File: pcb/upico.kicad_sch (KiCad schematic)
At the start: 71 parts, among them J1 uConsoleEXT, J2 uPico Connect, J3 USB_C_Receptacle_USB2.0, J4 Camera, J5 uConsoleSpeaker, J6 uConsoleSpeaker, U1 W25Q32JVUX, U2 RP2040, U3 USBLC6-2P6, U4 USBLC6-2P6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

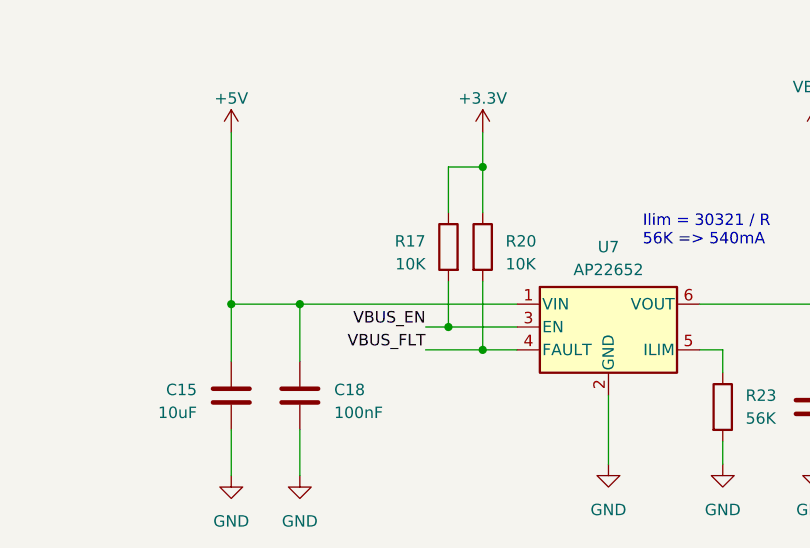
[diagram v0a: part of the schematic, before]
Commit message: invert power control signals
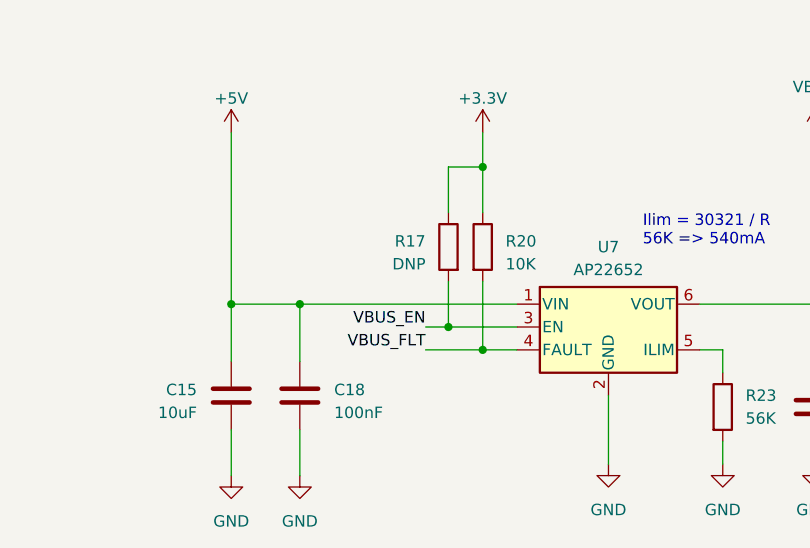
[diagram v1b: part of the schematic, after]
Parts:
- R17: value 10K -> DNP; PN C25744 -> (none)
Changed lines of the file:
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@@
       (effects (font (size 1.27 1.27)) (justify left))
     )
-    (property "Value" "10K" (at 340.36 55.245 0)
+    (property "Value" "DNP" (at 340.36 55.245 0)
       (effects (font (size 1.27 1.27)) (justify left))
     )
@@
       (effects (font (size 1.27 1.27)) hide)
     )
-    (property "PN" "C25744" (at 342.9 53.34 0)
+    (property "PN" "" (at 342.9 53.34 0)
       (effects (font (size 1.27 1.27)) hide)
     )

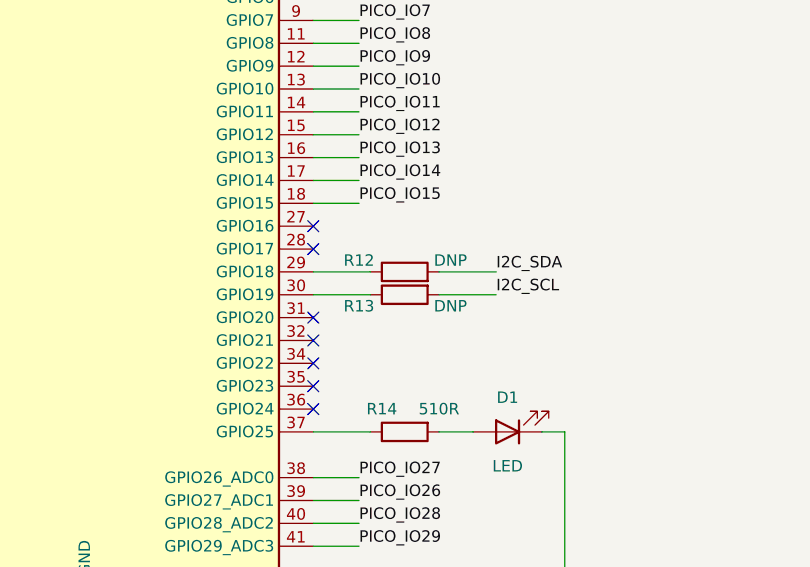
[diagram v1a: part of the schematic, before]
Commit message: pico auto mount
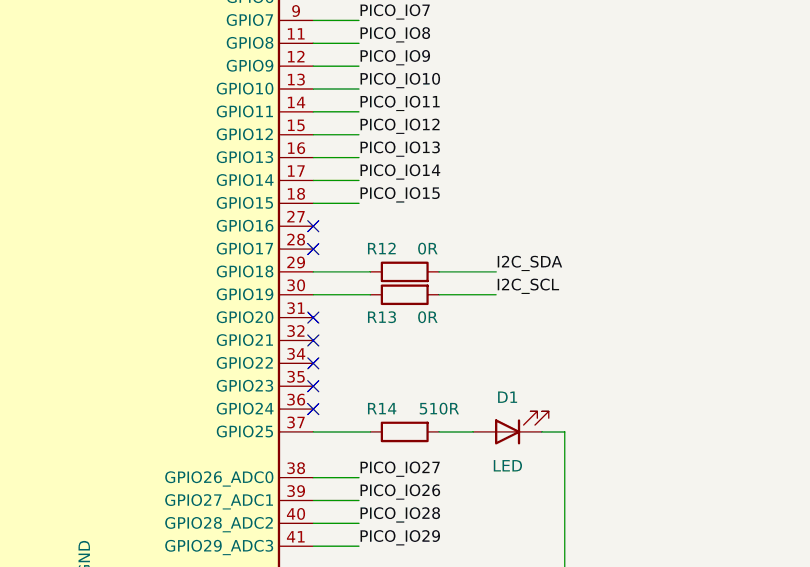
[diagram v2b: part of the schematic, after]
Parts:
- R12, R13: value DNP -> 0R
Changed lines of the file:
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@@
   (symbol (lib_id "Device:R") (at 138.43 215.9 90) (mirror x) (unit 1)
     (in_bom yes) (on_board yes) (dnp no)
-    (property "Reference" "R13" (at 133.35 217.17 90)
-      (effects (font (size 1.27 1.27)))
-    )
-    (property "Value" "DNP" (at 143.51 217.17 90)
+    (property "Reference" "R13" (at 135.89 218.44 90)
+      (effects (font (size 1.27 1.27)))
+    )
+    (property "Value" "0R" (at 140.97 218.44 90)
       (effects (font (size 1.27 1.27)))
     )
@@
   (symbol (lib_id "Device:R") (at 138.43 213.36 90) (unit 1)
     (in_bom yes) (on_board yes) (dnp no)
-    (property "Reference" "R12" (at 133.35 212.09 90)
-      (effects (font (size 1.27 1.27)))
-    )
-    (property "Value" "DNP" (at 143.51 212.09 90)
-      (effects (font (size 1.27 1.27)))
-    )
+    (property "Reference" "R12" (at 135.89 210.82 90)
+      (effects (font (size 1.27 1.27)))
+    )
+    (property "Value" "0R" (at 140.97 210.82 90)
+      (effects (font (size 1.27 1.27)))
+    )
